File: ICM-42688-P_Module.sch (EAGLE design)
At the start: 5 parts, among them P1 ICM-42688-P-MODULE-PINHEADER, U1 ICM-42688-P

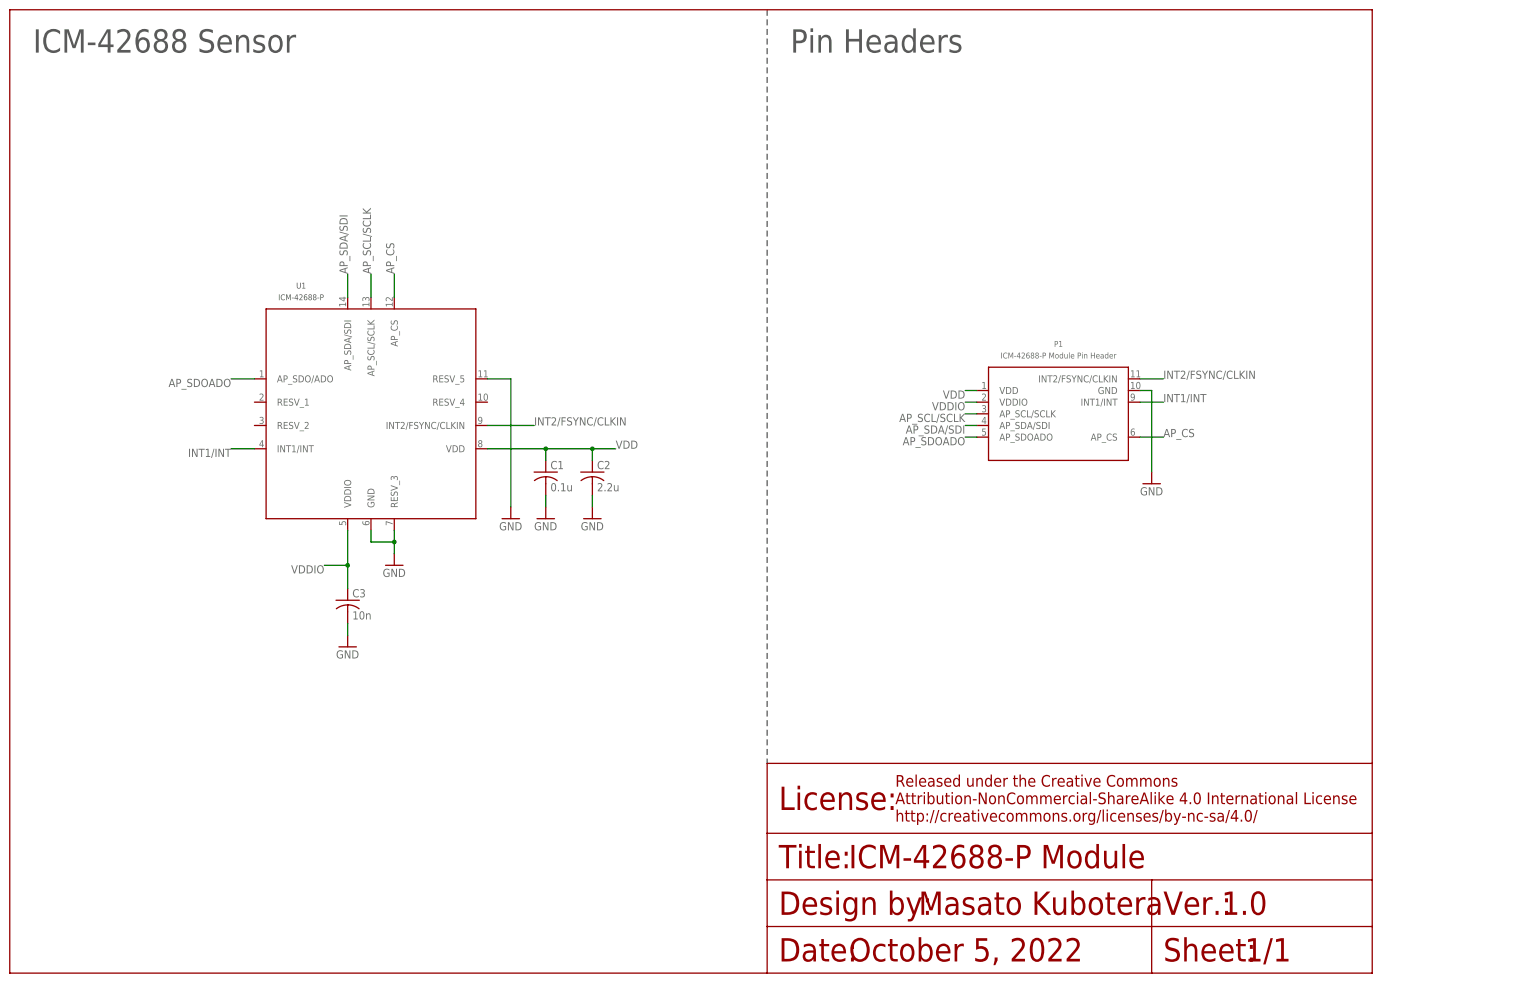
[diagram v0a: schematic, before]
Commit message: Update data for ordering
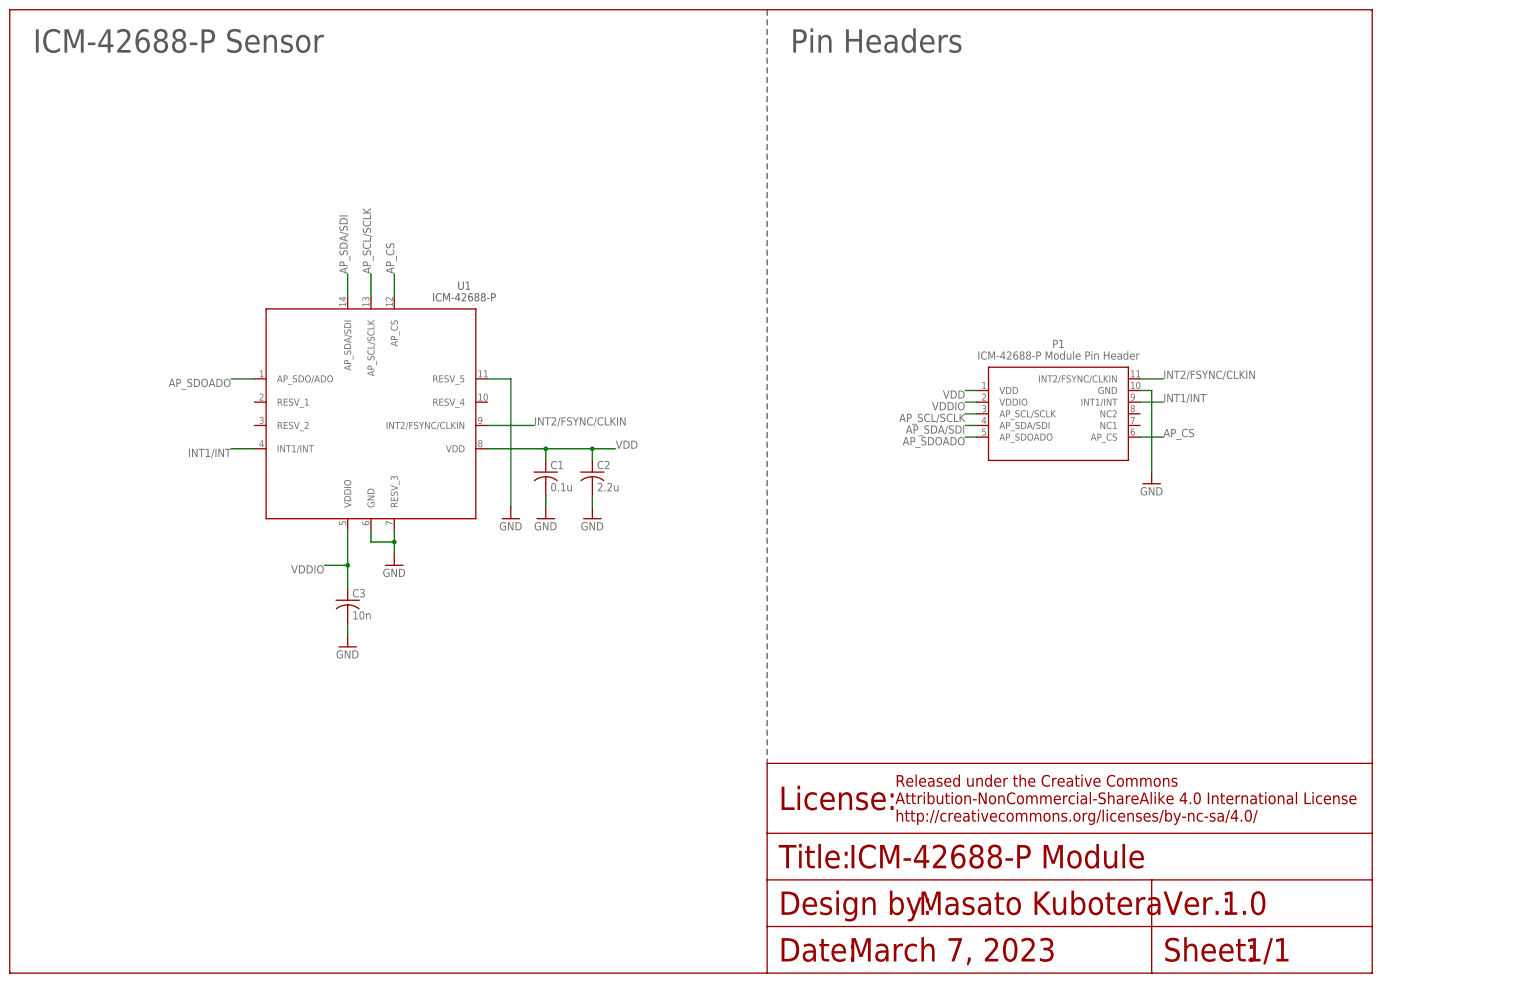
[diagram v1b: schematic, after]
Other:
- note added: "ICM-42688-P Sensor"
- note added: "March 7, 2023"
- note removed: "ICM-42688 Sensor"
- note removed: "October 5, 2022"
- moved on the sheet: U1
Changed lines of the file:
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@@
 <sheet>
 <plain>
-<text x="182.88" y="5.08" size="5.08" layer="94" font="vector" ratio="10" align="center-left">October 5, 2022</text>
+<text x="182.88" y="5.08" size="5.08" layer="94" font="vector" ratio="10" align="center-left">March 7, 2023</text>
 <text x="182.88" y="25.4" size="5.08" layer="94" font="vector" ratio="10" align="center-left">ICM-42688-P Module</text>
 <text x="264.16" y="15.24" size="5.08" layer="94" font="vector" ratio="10" align="center-left">1.0</text>
 <text x="269.24" y="5.08" size="5.08" layer="94" font="vector" ratio="10" align="center-left">1/1</text>
 <wire x1="165.1" y1="210" x2="165.1" y2="45.72" width="0.1524" layer="97" style="longdash"/>
-<text x="5.08" y="200.66" size="5.08" layer="97">ICM-42688 Sensor</text>
+<text x="5.08" y="200.66" size="5.08" layer="97">ICM-42688-P Sensor</text>
 <text x="170.18" y="200.66" size="5.08" layer="97">Pin Headers</text>
 </plain>
@@
 </instance>
 <instance part="P1" gate="G$1" x="228.6" y="121.92" smashed="yes">
-<attribute name="NAME" x="228.6" y="137.16" size="1.27" layer="95" font="vector" ratio="10" align="center"/>
+<attribute name="NAME" x="228.6" y="137.16" size="1.778" layer="95" font="vector" ratio="10" align="center"/>
 </instance>
 <instance part="GND1" gate="1" x="248.92" y="106.68" smashed="yes">
@@
 </instance>
 <instance part="U1" gate="G$1" x="78.74" y="121.92" smashed="yes">
-<attribute name="NAME" x="63.5" y="149.86" size="1.27" layer="97" font="vector" ratio="10" align="center"/>
+<attribute name="NAME" x="99.06" y="149.86" size="1.778" layer="97" font="vector" ratio="10" align="center"/>
 </instance>
 </instances>
